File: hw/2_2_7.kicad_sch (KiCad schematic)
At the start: 26 parts, among them U4 ATmega2560-16A, U5 AP64501SP-13

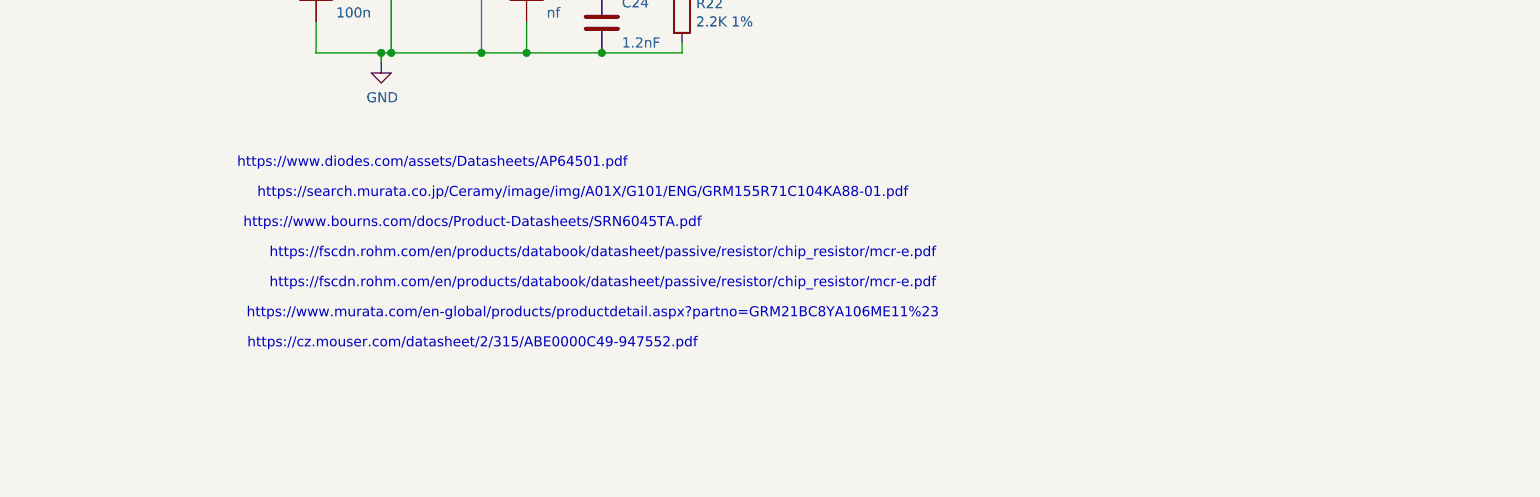
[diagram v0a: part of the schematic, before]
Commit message: Add LM2576S-5 to 2.3.10
Signed-off-by: ckalina <46683072+ckalina@users.noreply.github.com>
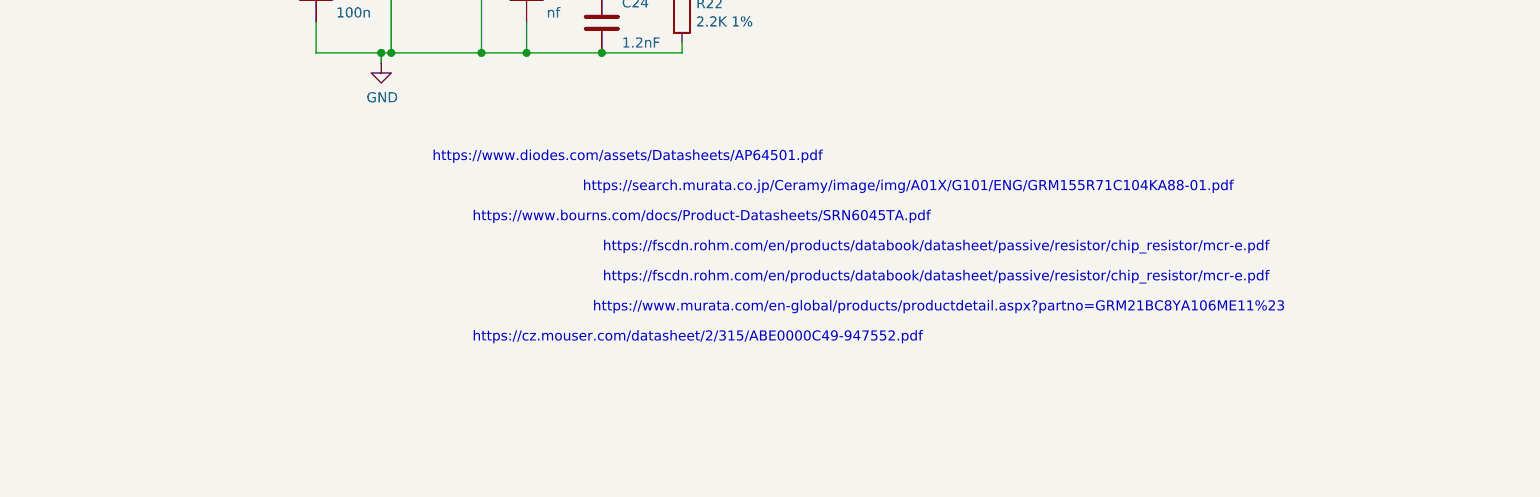
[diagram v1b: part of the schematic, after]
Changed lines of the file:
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@@
   (text "https://www.diodes.com/assets/Datasheets/AP64501.pdf"
     (at 176.53 109.22 0)
-    (effects (font (size 1.27 1.27)))
+    (effects (font (size 1.27 1.27)) (justify left bottom))
   )
   (text "https://www.bourns.com/docs/Product-Datasheets/SRN6045TA.pdf"
     (at 181.61 116.84 0)
-    (effects (font (size 1.27 1.27)))
+    (effects (font (size 1.27 1.27)) (justify left bottom))
   )
   (text "https://cz.mouser.com/datasheet/2/315/ABE0000C49-947552.pdf"
     (at 181.61 132.08 0)
-    (effects (font (size 1.27 1.27)))
+    (effects (font (size 1.27 1.27)) (justify left bottom))
   )
   (text "https://search.murata.co.jp/Ceramy/image/img/A01X/G101/ENG/GRM155R71C104KA88-01.pdf"
     (at 195.58 113.03 0)
-    (effects (font (size 1.27 1.27)))
+    (effects (font (size 1.27 1.27)) (justify left bottom))
   )
   (text "https://www.murata.com/en-global/products/productdetail.aspx?partno=GRM21BC8YA106ME11%23"
     (at 196.85 128.27 0)
-    (effects (font (size 1.27 1.27)))
+    (effects (font (size 1.27 1.27)) (justify left bottom))
   )
   (text "https://fscdn.rohm.com/en/products/databook/datasheet/passive/resistor/chip_resistor/mcr-e.pdf"
     (at 198.12 120.65 0)
-    (effects (font (size 1.27 1.27)))
+    (effects (font (size 1.27 1.27)) (justify left bottom))
   )
   (text "https://fscdn.rohm.com/en/products/databook/datasheet/passive/resistor/chip_resistor/mcr-e.pdf"
     (at 198.12 124.46 0)
-    (effects (font (size 1.27 1.27)))
+    (effects (font (size 1.27 1.27)) (justify left bottom))
   )
   (label "+5v" (at 36.83 31.75 180)
